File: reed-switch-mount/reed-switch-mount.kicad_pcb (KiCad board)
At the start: 2 copper layers, 116.8 x 15.2 mm, 28 parts, among them J1 CONN_02X05, SW1 SW_DIP_x01, SW2 SW_DIP_x01, SW3 SW_DIP_x01

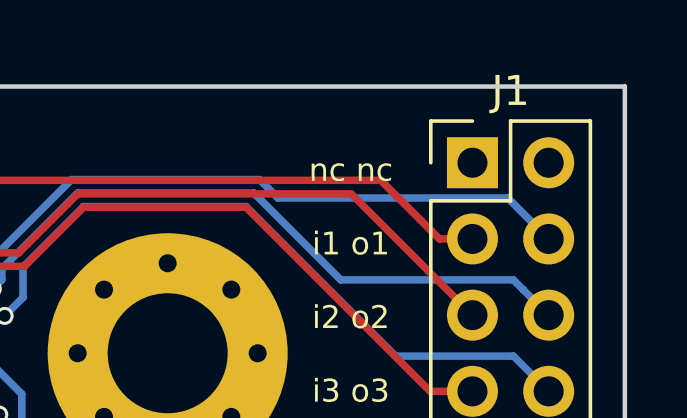
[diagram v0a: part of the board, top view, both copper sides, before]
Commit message: Corrected a number of footprint components
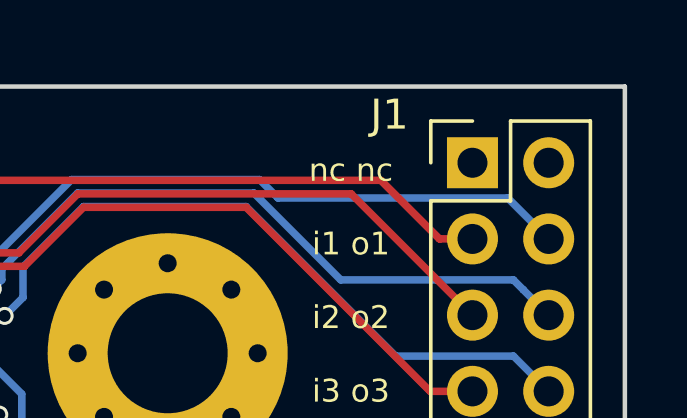
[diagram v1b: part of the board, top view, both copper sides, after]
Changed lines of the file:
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@@
 (kicad_pcb (version 4) (host pcbnew 4.0.6-e0-6349~53~ubuntu16.04.1)
   (general
-    (links 0)
-    (no_connects 8)
-    (area 91.364999 92.634999 208.355001 108.025001)
+    (links 45)
+    (no_connects 0)
+    (area 85.82 91.885 209.503334 108.9996)
     (thickness 1.6)
     (drawings 6)
@@
     (descr "Through hole straight pin header, 2x05, 2.54mm pitch, double rows")
     (tags "Through hole pin header THT 2x05 2.54mm double row")
-    (fp_text reference J1 (at 1.27 -2.39) (layer F.SilkS)
-      (effects (font (size 1 1) (thickness 0.15)))
-    )
+    (fp_text reference J1 (at -2.7686 -1.6002) (layer F.SilkS)
+      (effects (font (size 1 1) (thickness 0.15)))
+    )
